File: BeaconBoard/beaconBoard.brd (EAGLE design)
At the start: 101.6 x 76.2 mm, 32 parts, among them IC1 7805TV, Q1 2N3904

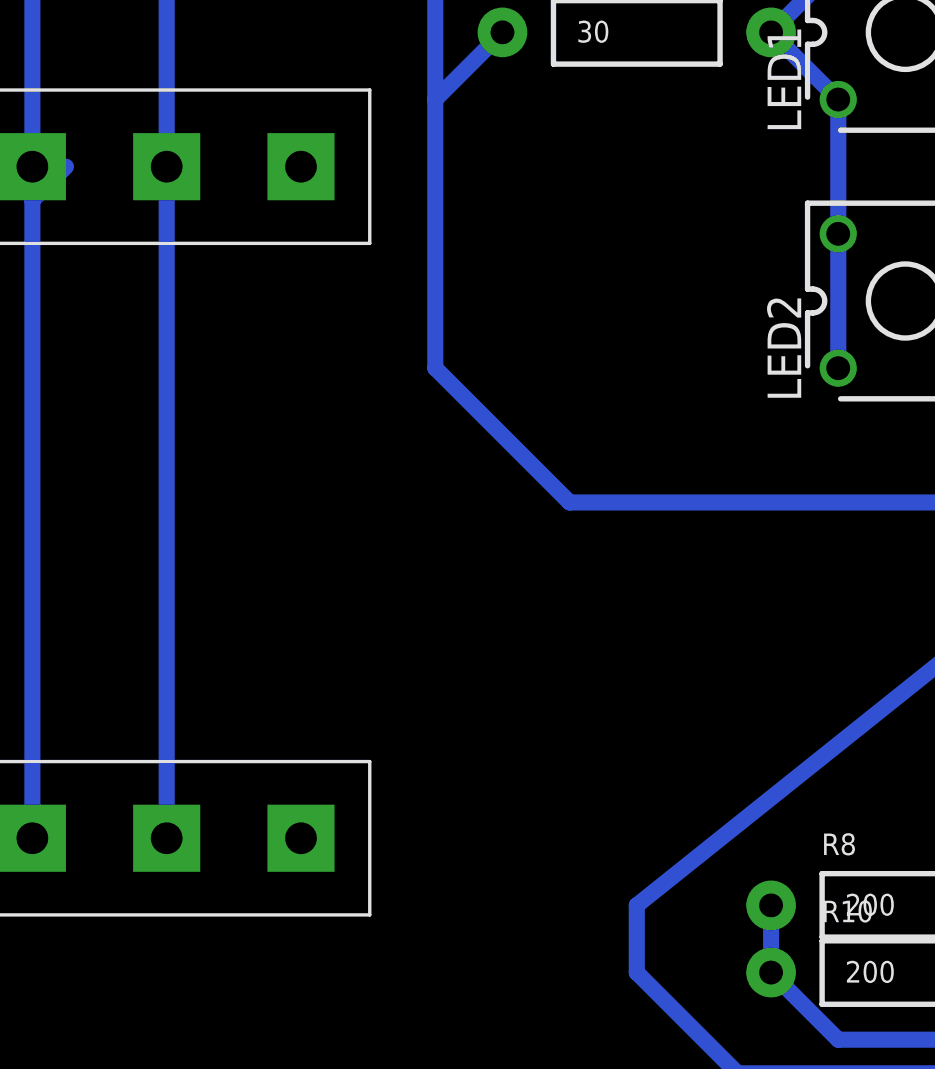
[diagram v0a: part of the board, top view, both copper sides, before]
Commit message: Add pull up resistor to bumpers
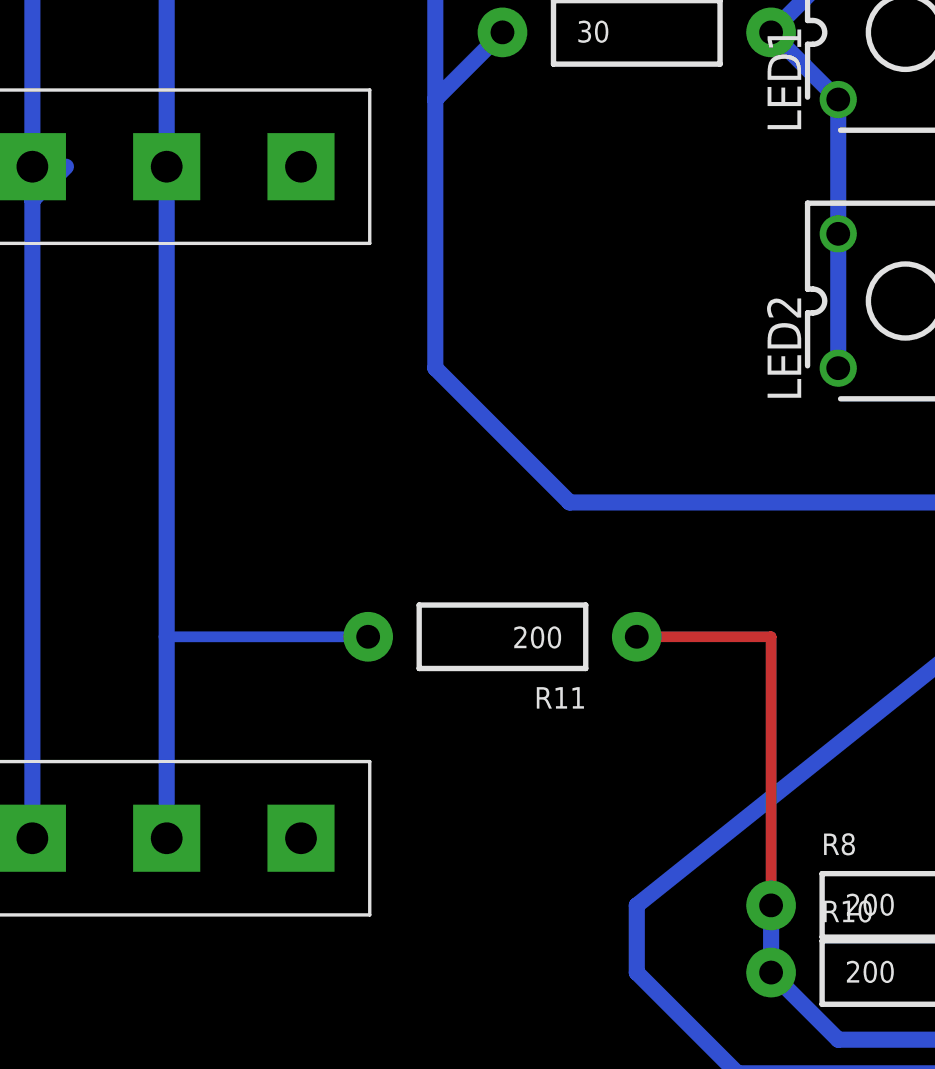
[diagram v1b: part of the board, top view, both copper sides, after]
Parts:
- added R11: 200, SparkFun-Resistors:AXIAL-0.4
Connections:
- net BUMPER: now also R11.P$2
- net VCC: now also R11.P$1
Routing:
- net VCC: track 185.5 -> 200.8 mm
- net BUMPER: track 120.7 -> 128.4 mm
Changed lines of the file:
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@@
 <element name="C6" library="SparkFun-Passives" package="CAP-PTH-SMALL" value="" x="71.12" y="35.56" rot="R270"/>
 <element name="JP2" library="SparkFun-Connectors" package="1X05_LOCK_LONGPADS" value="" x="82.55" y="16.51" rot="R270"/>
+<element name="R11" library="SparkFun-Resistors" package="AXIAL-0.4" value="200" x="22.86" y="20.32" rot="R180"/>
 </elements>
 <signals>
@@
 <wire x1="59.69" y1="6.35" x2="45.72" y2="6.35" width="0.6096" layer="16"/>
 <wire x1="45.72" y1="6.35" x2="44.45" y2="5.08" width="0.6096" layer="16"/>
+<contactref element="R11" pad="P$1"/>
+<wire x1="27.94" y1="20.32" x2="33.02" y2="20.32" width="0.4064" layer="1"/>
+<wire x1="33.02" y1="20.32" x2="33.02" y2="10.16" width="0.4064" layer="1"/>
 </signal>
 <signal name="GND">
@@
 <contactref element="U$2" pad="NO"/>
 <contactref element="U$3" pad="NO"/>
-<wire x1="10.16" y1="12.7" x2="10.16" y2="38.1" width="0.6096" layer="16"/>
+<wire x1="10.16" y1="12.7" x2="10.16" y2="20.32" width="0.6096" layer="16"/>
+<wire x1="10.16" y1="20.32" x2="10.16" y2="38.1" width="0.6096" layer="16"/>
 <wire x1="10.16" y1="63.5" x2="10.16" y2="38.1" width="0.6096" layer="16"/>
 <contactref element="U$4" pad="28"/>
@@
 <wire x1="15.24" y1="55.88" x2="10.16" y2="60.96" width="0.6096" layer="1"/>
 <wire x1="10.16" y1="60.96" x2="10.16" y2="63.5" width="0.6096" layer="1"/>
+<contactref element="R11" pad="P$2"/>
+<wire x1="17.78" y1="20.32" x2="10.16" y2="20.32" width="0.4064" layer="16"/>
 </signal>
 </signals>

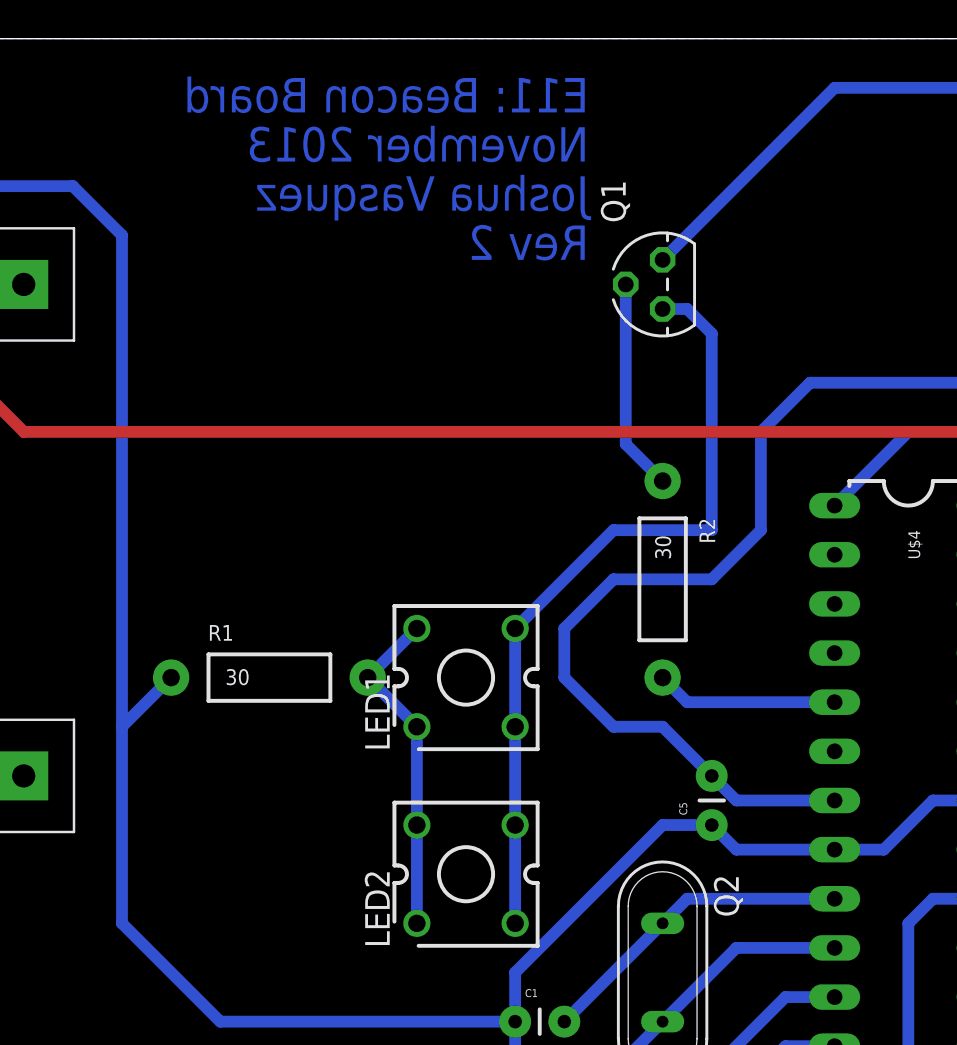
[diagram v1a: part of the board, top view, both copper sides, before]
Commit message: Move leds above npn transistor
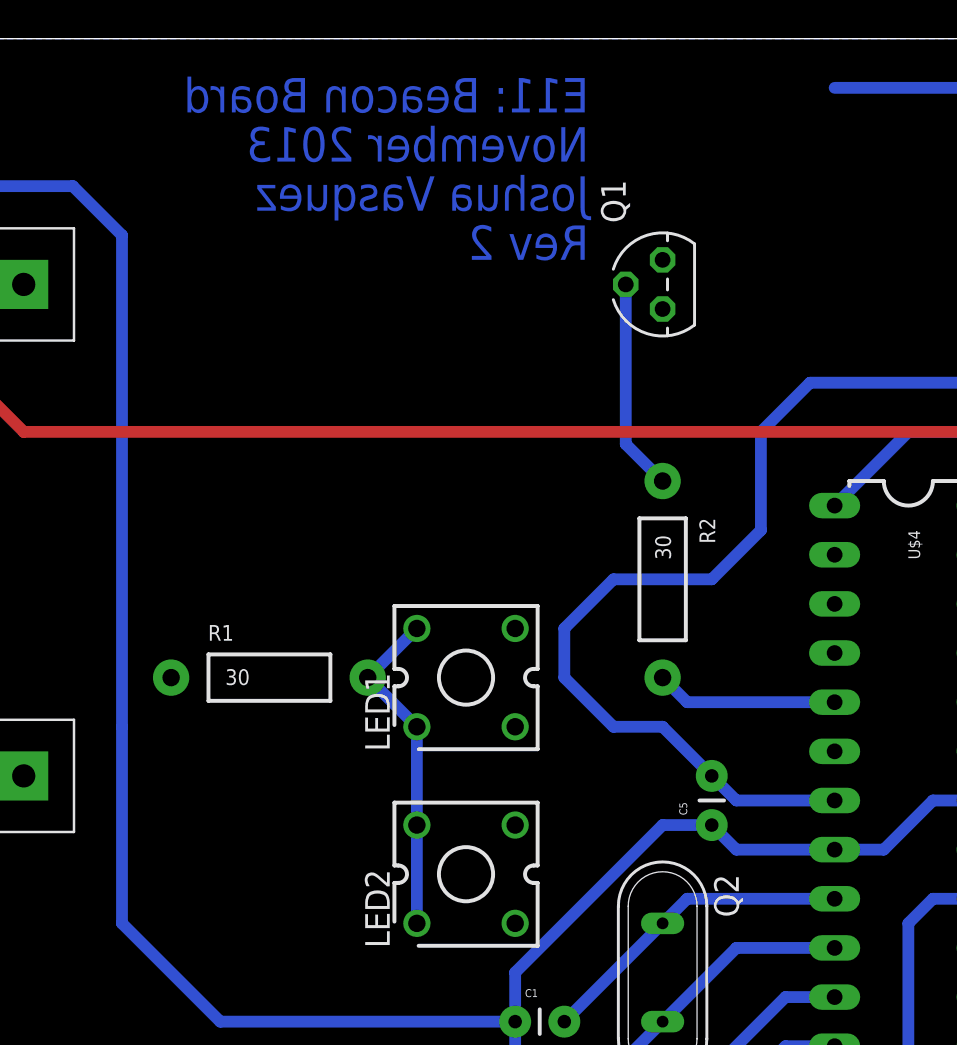
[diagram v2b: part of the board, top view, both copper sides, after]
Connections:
- net GND: now also Q1.E; no longer R1.P$1
- net N$1: now also Q1.C, R1.P$1; no longer LED1.2, LED1.3, LED2.2, LED2.3, Q1.E
- net VDD: now also LED1.2, LED1.3, LED2.2, LED2.3; no longer Q1.C
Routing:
- net N$1: track 40.7 -> 0.00 mm
- net VDD: track 37.0 -> 24.4 mm
- net GND: track 384.9 -> 381.3 mm
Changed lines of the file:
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@@
 <wire x1="69.85" y1="60.96" x2="68.58" y2="62.23" width="0.6096" layer="16"/>
 <wire x1="68.58" y1="62.23" x2="68.58" y2="66.04" width="0.6096" layer="16"/>
-<contactref element="R1" pad="P$1"/>
 <contactref element="LED5" pad="K"/>
 <contactref element="LED4" pad="K"/>
@@
 <wire x1="71.12" y1="35.56" x2="69.85" y2="36.83" width="0.6096" layer="16"/>
 <wire x1="69.85" y1="36.83" x2="68.8594" y2="36.83" width="0.6096" layer="16"/>
-<wire x1="22.86" y1="43.18" x2="20.32" y2="40.64" width="0.6096" layer="16"/>
 <wire x1="20.32" y1="40.64" x2="20.32" y2="30.48" width="0.6096" layer="16"/>
 <wire x1="20.32" y1="30.48" x2="25.4" y2="25.4" width="0.6096" layer="16"/>
@@
 <vertex x="0" y="0"/>
 </polygon>
+<contactref element="Q1" pad="E"/>
+<wire x1="68.58" y1="62.23" x2="48.26" y2="62.23" width="0" layer="19" extent="16-16"/>
+<wire x1="5.08" y1="36.83" x2="5.08" y2="38.1" width="0" layer="19" extent="16-16"/>
 </signal>
 <signal name="VDD">
@@
 <wire x1="78.74" y1="68.58" x2="76.2" y2="71.12" width="0.6096" layer="16"/>
 <wire x1="76.2" y1="71.12" x2="72.39" y2="71.12" width="0.6096" layer="16"/>
-<contactref element="Q1" pad="C"/>
-<wire x1="48.26" y1="64.77" x2="57.15" y2="73.66" width="0.6096" layer="16"/>
 <wire x1="57.15" y1="73.66" x2="71.12" y2="73.66" width="0.6096" layer="16"/>
 <wire x1="72.39" y1="71.12" x2="72.39" y2="72.39" width="0.6096" layer="16"/>
 <wire x1="72.39" y1="72.39" x2="71.12" y2="73.66" width="0.6096" layer="16"/>
-</signal>
-<signal name="N$1">
-<contactref element="Q1" pad="E"/>
 <contactref element="LED1" pad="2"/>
 <contactref element="LED1" pad="3"/>
 <contactref element="LED2" pad="2"/>
 <contactref element="LED2" pad="3"/>
-<wire x1="40.64" y1="45.72" x2="45.72" y2="50.8" width="0.6096" layer="16"/>
-<wire x1="45.72" y1="50.8" x2="50.8" y2="50.8" width="0.6096" layer="16"/>
-<wire x1="50.8" y1="50.8" x2="50.8" y2="60.96" width="0.6096" layer="16"/>
-<wire x1="50.8" y1="60.96" x2="49.53" y2="62.23" width="0.6096" layer="16"/>
-<wire x1="49.53" y1="62.23" x2="48.26" y2="62.23" width="0.6096" layer="16"/>
-<wire x1="40.64" y1="30.48" x2="40.64" y2="35.56" width="0.6096" layer="16"/>
-<wire x1="40.64" y1="35.56" x2="40.64" y2="40.64" width="0.6096" layer="16"/>
-<wire x1="40.64" y1="40.64" x2="40.64" y2="45.72" width="0.6096" layer="16"/>
+<wire x1="40.64" y1="45.72" x2="57.15" y2="73.66" width="0" layer="19" extent="16-16"/>
+<wire x1="40.64" y1="40.64" x2="40.64" y2="45.72" width="0" layer="19" extent="1-1"/>
+<wire x1="40.64" y1="35.56" x2="40.64" y2="40.64" width="0" layer="19" extent="1-1"/>
+<wire x1="40.64" y1="30.48" x2="40.64" y2="35.56" width="0" layer="19" extent="1-1"/>
 </signal>
 <signal name="N$3">
@@
 <wire x1="17.78" y1="20.32" x2="10.16" y2="20.32" width="0.4064" layer="16"/>
 </signal>
+<signal name="N$1">
+<contactref element="Q1" pad="C"/>
+<contactref element="R1" pad="P$1"/>
+<wire x1="22.86" y1="43.18" x2="48.26" y2="64.77" width="0" layer="19" extent="1-1"/>
+</signal>
 </signals>
